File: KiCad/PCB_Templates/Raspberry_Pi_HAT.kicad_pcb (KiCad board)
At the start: 2 copper layers, 65 x 56.5 mm, 5 parts

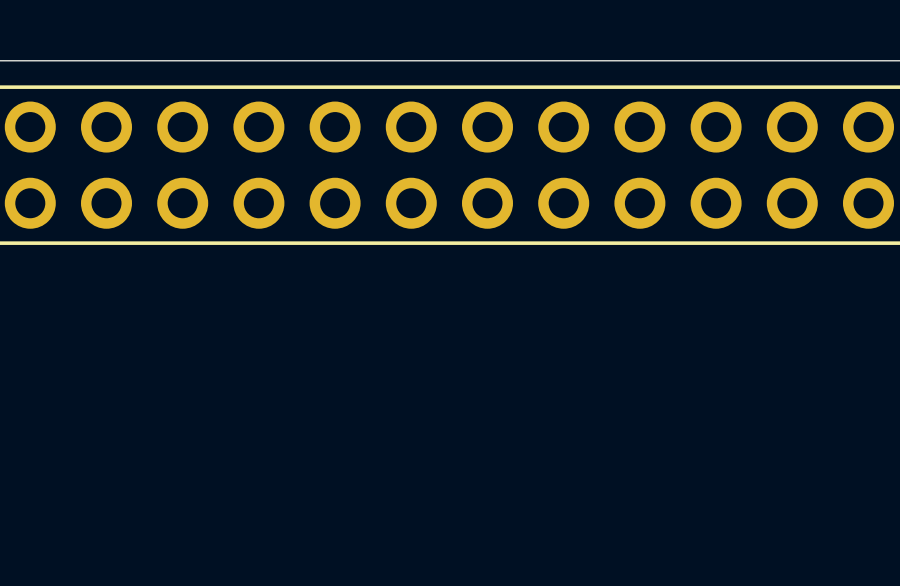
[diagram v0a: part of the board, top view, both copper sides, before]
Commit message: Make the RPI connector J1.
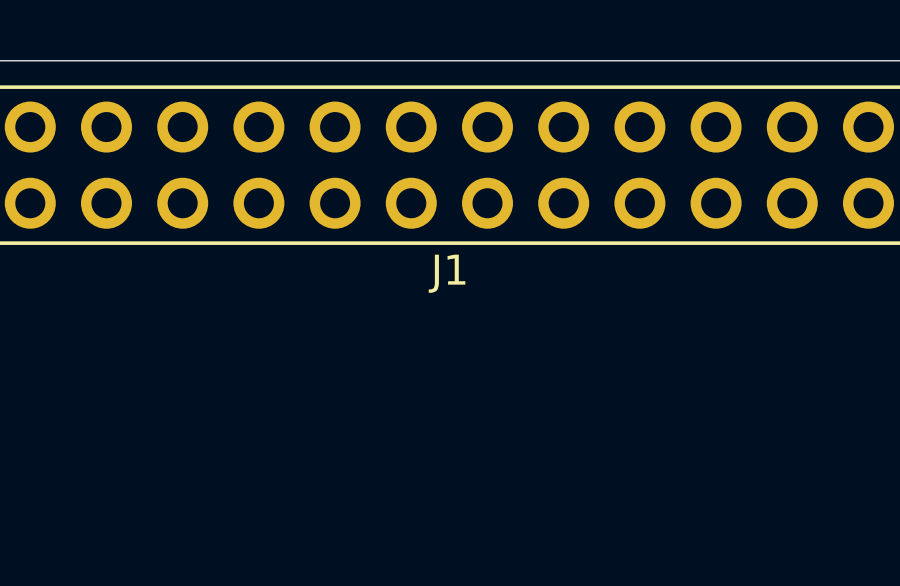
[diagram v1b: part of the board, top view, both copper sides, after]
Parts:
- renumbered REF** to J1
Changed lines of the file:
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@@
     (descr "Through hole straight pin header, 2x20, 2.54mm pitch, double rows")
     (tags "Through hole pin header THT 2x20 2.54mm double row")
-    (fp_text reference REF** (at 1.27 -2.33 90) (layer F.SilkS) hide
+    (fp_text reference J1 (at -2.25 24.15 180) (layer F.SilkS)
       (effects (font (size 1 1) (thickness 0.15)))
     )
